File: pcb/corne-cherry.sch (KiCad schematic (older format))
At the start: 144 parts, among them J1 MJ-4PP-9, J2 OLED, J3 MJ-4PP-9, J4 OLED, J5 Conn_01x01_Male, J6 Conn_01x01_Male, P1 Conn_01x03, P3 Conn_01x03, SW1 SW_PUSH, SW10 SW_PUSH, SW11 SW_PUSH, SW12 SW_PUSH, SW13 SW_PUSH, SW14 SW_PUSH, SW15 SW_PUSH, SW16 SW_PUSH, SW17 SW_PUSH, SW18 SW_PUSH, SW19 SW_PUSH, SW2 SW_PUSH, SW20 SW_PUSH, SW21 SW_PUSH, SW22 SW_PUSH, SW23 SW_PUSH, SW24 SW_PUSH, SW25 SW_PUSH, SW26 SW_PUSH, SW27 SW_PUSH, SW28 SW_PUSH, SW29 SW_PUSH, SW3 SW_PUSH, SW30 SW_PUSH, SW31 SW_PUSH, SW32 SW_PUSH, SW33 SW_PUSH, SW34 SW_PUSH, SW35 SW_PUSH, SW36 SW_PUSH, SW37 SW_PUSH, SW38 SW_PUSH, SW39 SW_PUSH, SW4 SW_PUSH, SW40 SW_PUSH, SW41 SW_PUSH, SW42 SW_PUSH, SW5 SW_PUSH, SW6 SW_PUSH, SW7 SW_PUSH, SW8 SW_PUSH, SW9 SW_PUSH, U1 ProMicro, U2 ProMicro

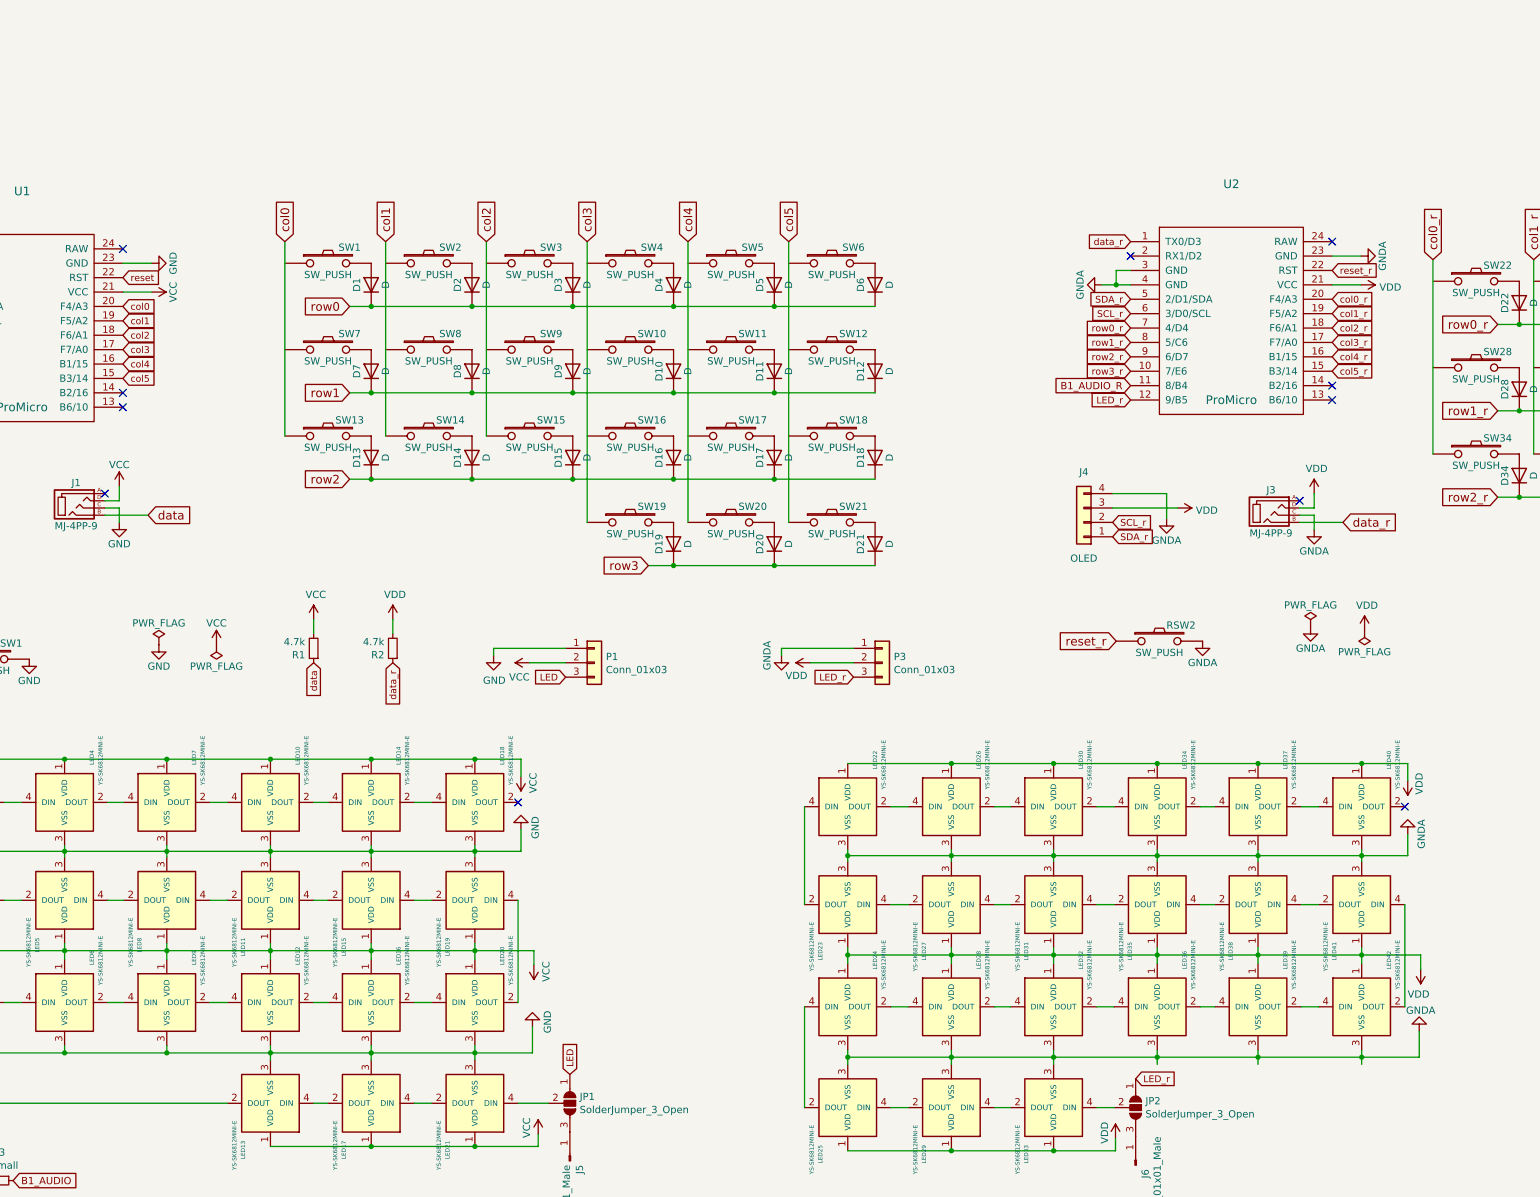
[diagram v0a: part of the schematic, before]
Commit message: Add encoder to left half
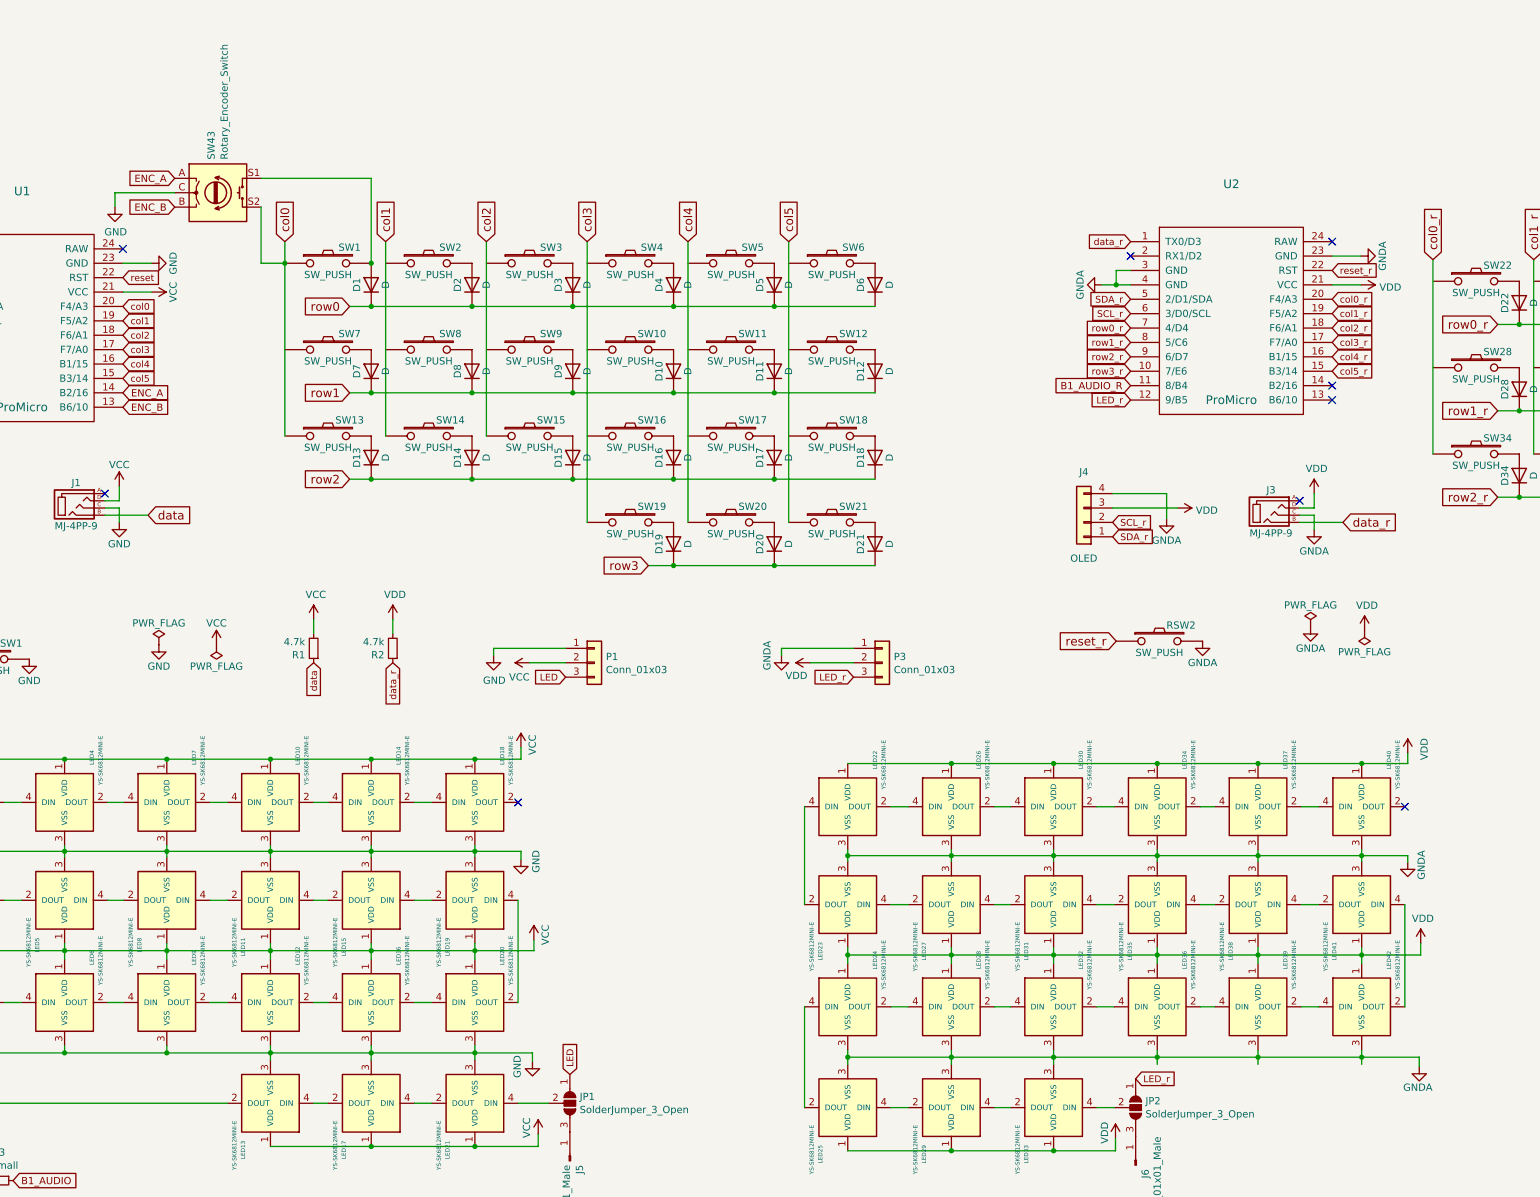
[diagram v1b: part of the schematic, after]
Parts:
- added SW43: Rotary_Encoder_Switch, Keebio-Parts:RotaryEncoder_EC11-no-legs, symbol Device:Rotary_Encoder_Switch
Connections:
- net GND: now also SW43.C
- net col0: now also SW1.1, SW43.S2
- net ENC_B: now reaches U1.13 (B6/10)
- net ENC_B: now also SW43.B
- net ENC_A: now reaches U1.14 (B2/16)
- net ENC_A: now also SW43.A
- net at D1.2 (A), SW1.2: now also SW43.S1
- no-connect marks 15 -> 13
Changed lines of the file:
@@
 Text GLabel 2475 1575 2    47   Input ~ 0
 col0
-NoConn ~ 2475 2175
 Text GLabel 1075 1575 0    47   Input ~ 0
 SDA
@@
 	9725 2875 9725 3050
 Wire Wire Line
-	3600 1125 3600 2475
+	3600 1125 3600 1275
 Wire Wire Line
 	4300 1125 4300 2475
@@
 $EndComp
 $Comp
-L kbd:YS-SK6812MINI-E LED20
-U 1 1 60615E90
-P 4920 6410
-F 0 "LED20" V 5110 6670 29  0000 L CNN
-F 1 "YS-SK6812MINI-E" V 5170 6530 29  0000 L CNN
-F 2 "kbd:YS-SK6812MINI-E" H 5020 6160 50  0001 C CNN
-F 3 "" H 5020 6160 50  0001 C CNN
-	1    4920 6410
-	1    0    0    -1
-$EndComp
-$Comp
 L kbd:YS-SK6812MINI-E LED16
 U 1 1 60615E86
@@
 	1350 5360 2070 5360
 Wire Wire Line
-	5240 5360 5240 5210
-Wire Wire Line
 	4920 5320 4920 5360
 Connection ~ 4920 5360
@@
 Wire Wire Line
 	1350 4720 2070 4720
-Wire Wire Line
-	5240 4720 5240 4840
 Connection ~ 2070 4720
 Wire Wire Line
@@
 L power:VCC #PWR0107
 U 1 1 607BF7C1
-P 5240 4840
-F 0 "#PWR0107" H 5240 4690 50  0001 C CNN
-F 1 "VCC" V 5155 4885 50  0000 C CNN
-F 2 "" H 5240 4840 50  0001 C CNN
-F 3 "" H 5240 4840 50  0001 C CNN
-	1    5240 4840
-	-1   0    0    1
+P 5240 4640
+F 0 "#PWR0107" H 5240 4490 50  0001 C CNN
+F 1 "VCC" V 5320 4660 50  0000 C CNN
+F 2 "" H 5240 4640 50  0001 C CNN
+F 3 "" H 5240 4640 50  0001 C CNN
+	1    5240 4640
+	1    0    0    -1
 $EndComp
 $Comp
 L power:GND #PWR0108
 U 1 1 607C08F0
-P 5240 5210
-F 0 "#PWR0108" H 5240 4960 50  0001 C CNN
-F 1 "GND" V 5140 5195 50  0000 C CNN
-F 2 "" H 5240 5210 50  0001 C CNN
-F 3 "" H 5240 5210 50  0001 C CNN
-	1    5240 5210
-	-1   0    0    1
+P 5240 5415
+F 0 "#PWR0108" H 5240 5165 50  0001 C CNN
+F 1 "GND" V 5345 5400 50  0000 C CNN
+F 2 "" H 5240 5415 50  0001 C CNN
+F 3 "" H 5240 5415 50  0001 C CNN
+	1    5240 5415
+	1    0    0    -1
 $EndComp
 Wire Wire Line
 	1350 6050 2070 6050
-Wire Wire Line
-	5330 6050 5330 6150
 Wire Wire Line
 	1350 6710 1350 6760
@@
 Wire Wire Line
 	4920 6760 5320 6760
-Wire Wire Line
-	5320 6760 5320 6580
 $Comp
 L power:VCC #PWR0109
 U 1 1 60A1725F
-P 5330 6150
-F 0 "#PWR0109" H 5330 6000 50  0001 C CNN
-F 1 "VCC" V 5245 6195 50  0000 C CNN
-F 2 "" H 5330 6150 50  0001 C CNN
-F 3 "" H 5330 6150 50  0001 C CNN
-	1    5330 6150
-	-1   0    0    1
-$EndComp
-$Comp
-L power:GND #PWR0110
-U 1 1 60A183F3
-P 5320 6580
-F 0 "#PWR0110" H 5320 6330 50  0001 C CNN
-F 1 "GND" V 5215 6545 50  0000 C CNN
-F 2 "" H 5320 6580 50  0001 C CNN
-F 3 "" H 5320 6580 50  0001 C CNN
-	1    5320 6580
-	-1   0    0    1
+P 5330 5975
+F 0 "#PWR0109" H 5330 5825 50  0001 C CNN
+F 1 "VCC" V 5410 6010 50  0000 C CNN
+F 2 "" H 5330 5975 50  0001 C CNN
+F 3 "" H 5330 5975 50  0001 C CNN
+	1    5330 5975
+	1    0    0    -1
 $EndComp
 Wire Wire Line
@@
 Wire Wire Line
 	7510 4750 8230 4750
-Wire Wire Line
-	11400 4750 11400 4870
 Connection ~ 8230 4750
 Wire Wire Line
@@
 	7510 6080 8230 6080
 Wire Wire Line
-	11490 6080 11490 6180
-Wire Wire Line
 	7510 6740 7510 6790
 Wire Wire Line
@@
 Wire Wire Line
 	11080 6790 11480 6790
-Wire Wire Line
-	11480 6790 11480 6610
 Wire Wire Line
 	10780 6440 10660 6440
@@
 L power:VDD #PWR0112
 U 1 1 60837821
-P 11490 6180
-F 0 "#PWR0112" H 11490 6030 50  0001 C CNN
-F 1 "VDD" H 11505 6353 50  0000 C CNN
-F 2 "" H 11490 6180 50  0001 C CNN
-F 3 "" H 11490 6180 50  0001 C CNN
-	1    11490 6180
-	-1   0    0    1
+P 11490 6000
+F 0 "#PWR0112" H 11490 5850 50  0001 C CNN
+F 1 "VDD" H 11505 6173 50  0000 C CNN
+F 2 "" H 11490 6000 50  0001 C CNN
+F 3 "" H 11490 6000 50  0001 C CNN
+	1    11490 6000
+	1    0    0    -1
 $EndComp
 $Comp
 L power:GNDA #PWR0115
 U 1 1 60878D51
-P 11480 6610
-F 0 "#PWR0115" H 11480 6360 50  0001 C CNN
-F 1 "GNDA" H 11470 6465 50  0000 C CNN
-F 2 "" H 11480 6610 50  0001 C CNN
-F 3 "" H 11480 6610 50  0001 C CNN
-	1    11480 6610
-	-1   0    0    1
-$EndComp
-$Comp
-L power:GNDA #PWR0116
-U 1 1 6087A621
-P 11400 5240
-F 0 "#PWR0116" H 11400 4990 50  0001 C CNN
-F 1 "GNDA" V 11305 5240 50  0000 C CNN
-F 2 "" H 11400 5240 50  0001 C CNN
-F 3 "" H 11400 5240 50  0001 C CNN
-	1    11400 5240
-	-1   0    0    1
+P 11480 6855
+F 0 "#PWR0115" H 11480 6605 50  0001 C CNN
+F 1 "GNDA" H 11470 6710 50  0000 C CNN
+F 2 "" H 11480 6855 50  0001 C CNN
+F 3 "" H 11480 6855 50  0001 C CNN
+	1    11480 6855
+	1    0    0    -1
 $EndComp
 $Comp
@@
 	1    0    0    -1
 $EndComp
-NoConn ~ 2475 2275
 $Comp
 L kbd:ProMicro U2
@@
 	9370 7440 9370 7355
 $Comp
-L power:VDD #PWR?
+L power:VDD #PWR0111
 U 1 1 6082E68A
 P 9370 7355
-F 0 "#PWR?" H 9370 7205 50  0001 C CNN
+F 0 "#PWR0111" H 9370 7205 50  0001 C CNN
 F 1 "VDD" V 9295 7395 50  0000 C CNN
 F 2 "" H 9370 7355 50  0001 C CNN
@@
 	0    1    1    0
 $EndComp
-Wire Wire Line
-	11400 5390 11400 5240
-Wire Wire Line
-	10360 4750 11080 4750
-Wire Wire Line
-	11080 4750 11400 4750
-Connection ~ 11080 4750
 $Comp
 L power:VDD #PWR0114
 U 1 1 60838250
-P 11400 4870
-F 0 "#PWR0114" H 11400 4720 50  0001 C CNN
-F 1 "VDD" V 11320 4890 50  0000 C CNN
-F 2 "" H 11400 4870 50  0001 C CNN
-F 3 "" H 11400 4870 50  0001 C CNN
-	1    11400 4870
-	-1   0    0    1
-$EndComp
+P 11400 4680
+F 0 "#PWR0114" H 11400 4530 50  0001 C CNN
+F 1 "VDD" V 11515 4710 50  0000 C CNN
+F 2 "" H 11400 4680 50  0001 C CNN
+F 3 "" H 11400 4680 50  0001 C CNN
+	1    11400 4680
+	1    0    0    -1
+$EndComp
+Wire Wire Line
+	5360 7410 5360 7325
+$Comp
+L power:VCC #PWR0113
+U 1 1 6098BE6F
+P 5360 7325
+F 0 "#PWR0113" H 5360 7175 50  0001 C CNN
+F 1 "VCC" V 5280 7370 50  0000 C CNN
+F 2 "" H 5360 7325 50  0001 C CNN
+F 3 "" H 5360 7325 50  0001 C CNN
+	1    5360 7325
+	1    0    0    -1
+$EndComp
+$Comp
+L power:GND #PWR0110
+U 1 1 60A183F3
+P 5320 6820
+F 0 "#PWR0110" H 5320 6570 50  0001 C CNN
+F 1 "GND" V 5215 6785 50  0000 C CNN
+F 2 "" H 5320 6820 50  0001 C CNN
+F 3 "" H 5320 6820 50  0001 C CNN
+	1    5320 6820
+	1    0    0    -1
+$EndComp
+$Comp
+L kbd:YS-SK6812MINI-E LED20
+U 1 1 60615E90
+P 4920 6410
+F 0 "LED20" V 5110 6670 29  0000 L CNN
+F 1 "YS-SK6812MINI-E" V 5170 6530 29  0000 L CNN
+F 2 "kbd:YS-SK6812MINI-E" H 5020 6160 50  0001 C CNN
+F 3 "" H 5020 6160 50  0001 C CNN
+	1    4920 6410
+	1    0    0    -1
+$EndComp
+Wire Wire Line
+	5320 6760 5320 6820
+Wire Wire Line
+	5330 6050 5330 5975
+Wire Wire Line
+	5240 5360 5240 5415
+Wire Wire Line
+	5240 4720 5240 4640
+Wire Wire Line
+	11480 6855 11480 6790
+Wire Wire Line
+	11490 6080 11490 6000
+Connection ~ 11080 4750
+Wire Wire Line
+	11080 4750 11400 4750
+Wire Wire Line
+	10360 4750 11080 4750
 $Comp
 L kbd:YS-SK6812MINI-E LED40
@@
 	1    0    0    -1
 $EndComp
-Wire Wire Line
-	5360 7410 5360 7325
-$Comp
-L power:VCC #PWR?
-U 1 1 6098BE6F
-P 5360 7325
-F 0 "#PWR?" H 5360 7175 50  0001 C CNN
-F 1 "VCC" V 5280 7370 50  0000 C CNN
-F 2 "" H 5360 7325 50  0001 C CNN
-F 3 "" H 5360 7325 50  0001 C CNN
-	1    5360 7325
-	1    0    0    -1
-$EndComp
+$Comp
+L power:GNDA #PWR0116
+U 1 1 6087A621
+P 11400 5435
+F 0 "#PWR0116" H 11400 5185 50  0001 C CNN
+F 1 "GNDA" V 11495 5415 50  0000 C CNN
+F 2 "" H 11400 5435 50  0001 C CNN
+F 3 "" H 11400 5435 50  0001 C CNN
+	1    11400 5435
+	1    0    0    -1
+$EndComp
+Wire Wire Line
+	11400 5390 11400 5435
+Wire Wire Line
+	11400 4750 11400 4680
+$Comp
+L Device:Rotary_Encoder_Switch SW43
+U 1 1 6078866B
+P 3135 785
+F 0 "SW43" V 3089 1015 50  0000 L CNN
+F 1 "Rotary_Encoder_Switch" V 3180 1015 50  0000 L CNN
+F 2 "Keebio-Parts:RotaryEncoder_EC11-no-legs" H 2985 945 50  0001 C CNN
+F 3 "~" H 3135 1045 50  0001 C CNN
+	1    3135 785
+	1    0    0    -1
+$EndComp
+Wire Wire Line
+	2835 785  2420 785
+Wire Wire Line
+	2420 785  2420 885
+$Comp
+L power:GND #PWR?
+U 1 1 60823858
+P 2420 885
+F 0 "#PWR?" H 2420 635 50  0001 C CNN
+F 1 "GND" H 2425 712 50  0000 C CNN
+F 2 "" H 2420 885 50  0001 C CNN
+F 3 "" H 2420 885 50  0001 C CNN
+	1    2420 885
+	1    0    0    -1
+$EndComp
+Text GLabel 2835 685  0    50   Input ~ 0
+ENC_A
+Text GLabel 2835 885  0    50   Input ~ 0
+ENC_B
+Text GLabel 2475 2275 2    50   Input ~ 0
+ENC_B
+Text GLabel 2475 2175 2    50   Input ~ 0
+ENC_A
+Wire Wire Line
+	3435 885  3435 1275
+Wire Wire Line
+	3435 1275 3600 1275
+Connection ~ 3600 1275
+Wire Wire Line
+	3600 1275 3600 2475
+Wire Wire Line
+	3435 685  4200 685
+Wire Wire Line
+	4200 685  4200 1275
+Connection ~ 4200 1275
 $EndSCHEMATC

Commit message: Finish PCB
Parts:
- added SW44: Rotary_Encoder_Switch, Keebio-Parts:RotaryEncoder_EC11-no-legs, symbol Device:Rotary_Encoder_Switch
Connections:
- net GNDA: now also SW44.C
- net col0_r: now also SW22.1, SW44.S2
- net ENC_B_R: now reaches U2.13 (B6/10)
- net ENC_B_R: now also SW44.B
- net ENC_A_R: now reaches U2.14 (B2/16)
- net ENC_A_R: now also SW44.A
- net at D22.2 (A), SW22.2: now also SW44.S1
- no-connect marks 13 -> 11
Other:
- moved on the sheet: U2
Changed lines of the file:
@@
 L power:GNDA #PWR017
 U 1 1 5C25F963
-P 11075 1225
-F 0 "#PWR017" H 11075 975 50  0001 C CNN
-F 1 "GNDA" H 11075 1075 50  0000 C CNN
-F 2 "" H 11075 1225 50  0001 C CNN
-F 3 "" H 11075 1225 50  0001 C CNN
-	1    11075 1225
+P 10105 1250
+F 0 "#PWR017" H 10105 1000 50  0001 C CNN
+F 1 "GNDA" H 10105 1100 50  0000 C CNN
+F 2 "" H 10105 1250 50  0001 C CNN
+F 3 "" H 10105 1250 50  0001 C CNN
+	1    10105 1250
 	0    -1   -1   0
 $EndComp
@@
 L power:GNDA #PWR018
 U 1 1 5C25F969
-P 9275 1425
-F 0 "#PWR018" H 9275 1175 50  0001 C CNN
-F 1 "GNDA" H 9275 1275 50  0000 C CNN
-F 2 "" H 9275 1425 50  0001 C CNN
-F 3 "" H 9275 1425 50  0001 C CNN
-	1    9275 1425
+P 8305 1450
+F 0 "#PWR018" H 8305 1200 50  0001 C CNN
+F 1 "GNDA" H 8305 1300 50  0000 C CNN
+F 2 "" H 8305 1450 50  0001 C CNN
+F 3 "" H 8305 1450 50  0001 C CNN
+	1    8305 1450
 	0    1    1    0
 $EndComp
-Text GLabel 10875 1625 2    47   Input ~ 0
+Text GLabel 9905 1650 2    47   Input ~ 0
 col1_r
-Text GLabel 10875 1725 2    47   Input ~ 0
+Text GLabel 9905 1750 2    47   Input ~ 0
 col2_r
-Text GLabel 10875 1825 2    47   Input ~ 0
+Text GLabel 9905 1850 2    47   Input ~ 0
 col3_r
-Text GLabel 10875 1925 2    47   Input ~ 0
+Text GLabel 9905 1950 2    47   Input ~ 0
 col4_r
-Text GLabel 10875 2025 2    47   Input ~ 0
+Text GLabel 9905 2050 2    47   Input ~ 0
 col5_r
-Text GLabel 9475 2025 0    47   Input ~ 0
+Text GLabel 8505 2050 0    47   Input ~ 0
 row3_r
-Text GLabel 9475 1925 0    47   Input ~ 0
+Text GLabel 8505 1950 0    47   Input ~ 0
 row2_r
-Text GLabel 9475 1825 0    47   Input ~ 0
+Text GLabel 8505 1850 0    47   Input ~ 0
 row1_r
-Text GLabel 9475 1725 0    47   Input ~ 0
+Text GLabel 8505 1750 0    47   Input ~ 0
 row0_r
 $Comp
@@
 	1    0    0    -1
 $EndComp
-Text GLabel 9475 2225 0    47   Input ~ 0
+Text GLabel 8505 2250 0    47   Input ~ 0
 LED_r
-Text GLabel 9475 1125 0    47   Input ~ 0
+Text GLabel 8505 1150 0    47   Input ~ 0
 data_r
 $Comp
@@
 Text GLabel 10950 3075 2    60   Input ~ 0
 data_r
-Text GLabel 10875 1325 2    47   Input ~ 0
+Text GLabel 9905 1350 2    47   Input ~ 0
 reset_r
 Text GLabel 9375 3900 0    60   Input ~ 0
 reset_r
-NoConn ~ 9475 1225
-Text GLabel 10875 1525 2    47   Input ~ 0
+NoConn ~ 8505 1250
+Text GLabel 9905 1550 2    47   Input ~ 0
 col0_r
-NoConn ~ 10875 2125
-Text GLabel 9475 1525 0    47   Input ~ 0
+Text GLabel 8505 1550 0    47   Input ~ 0
 SDA_r
-Text GLabel 9475 1625 0    47   Input ~ 0
+Text GLabel 8505 1650 0    47   Input ~ 0
 SCL_r
 $Comp
@@
 Text GLabel 9350 3175 2    47   Input ~ 0
 SDA_r
-NoConn ~ 10875 1125
+NoConn ~ 9905 1150
 $Comp
 L kbd:MJ-4PP-9 J3
@@
 	12025 1700 12175 1700
 Wire Wire Line
-	9375 1325 9375 1425
-Connection ~ 9375 1425
-Wire Wire Line
-	9475 1325 9375 1325
-Wire Wire Line
-	9275 1425 9375 1425
+	8405 1350 8405 1450
+Connection ~ 8405 1450
+Wire Wire Line
+	8505 1350 8405 1350
+Wire Wire Line
+	8305 1450 8405 1450
 Connection ~ 12175 2900
 Connection ~ 12875 2900
@@
 Connection ~ 14975 1700
 Wire Wire Line
-	10875 1225 11075 1225
-Wire Wire Line
-	10875 1425 11075 1425
+	9905 1250 10105 1250
+Wire Wire Line
+	9905 1450 10105 1450
 Wire Wire Line
 	10650 3075 10950 3075
@@
 	14975 3500 15675 3500
 Wire Wire Line
-	9375 1425 9475 1425
+	8405 1450 8505 1450
 Wire Wire Line
 	12175 2900 12875 2900
@@
 L power:VDD #PWR019
 U 1 1 5C714C7F
-P 11075 1425
-F 0 "#PWR019" H 11075 1275 50  0001 C CNN
-F 1 "VDD" V 11092 1553 50  0000 L CNN
-F 2 "" H 11075 1425 50  0001 C CNN
-F 3 "" H 11075 1425 50  0001 C CNN
-	1    11075 1425
+P 10105 1450
+F 0 "#PWR019" H 10105 1300 50  0001 C CNN
+F 1 "VDD" V 10122 1578 50  0000 L CNN
+F 2 "" H 10105 1450 50  0001 C CNN
+F 3 "" H 10105 1450 50  0001 C CNN
+	1    10105 1450
 	0    1    1    0
 $EndComp
@@
 	5000 1125 5000 2475
 Wire Wire Line
-	11575 1250 11575 2600
+	11575 1250 11575 1400
 Wire Wire Line
 	12275 1250 12275 2600
@@
 L kbd:ProMicro U2
 U 1 1 5C25F857
-P 10175 1675
-F 0 "U2" H 10175 2625 60  0000 C CNN
-F 1 "ProMicro" H 10175 1125 60  0000 C CNN
-F 2 "kbd:ProMicro_v3" H 10275 625 60  0001 C CNN
-F 3 "" H 10275 625 60  0000 C CNN
-	1    10175 1675
-	1    0    0    -1
-$EndComp
-NoConn ~ 10875 2225
+P 9205 1700
+F 0 "U2" H 9205 2650 60  0000 C CNN
+F 1 "ProMicro" H 9205 1150 60  0000 C CNN
+F 2 "kbd:ProMicro_v3" H 9305 650 60  0001 C CNN
+F 3 "" H 9305 650 60  0000 C CNN
+	1    9205 1700
+	1    0    0    -1
+$EndComp
 NoConn ~ 5718 9687
 NoConn ~ 5470 8376
@@
 Wire Wire Line
 	7467 8158 7467 8302
-Text GLabel 9475 2125 0    50   Input ~ 0
+Text GLabel 8505 2150 0    50   Input ~ 0
 B1_AUDIO_R
 Text GLabel 1712 7647 2    50   Input ~ 0
@@
 	2420 785  2420 885
 $Comp
-L power:GND #PWR?
+L power:GND #PWR0119
 U 1 1 60823858
 P 2420 885
-F 0 "#PWR?" H 2420 635 50  0001 C CNN
+F 0 "#PWR0119" H 2420 635 50  0001 C CNN
 F 1 "GND" H 2425 712 50  0000 C CNN
 F 2 "" H 2420 885 50  0001 C CNN
@@
 	4200 685  4200 1275
 Connection ~ 4200 1275
+Text GLabel 9905 2150 2    50   Input ~ 0
+ENC_A_R
+Text GLabel 9905 2250 2    50   Input ~ 0
+ENC_B_R
+$Comp
+L Device:Rotary_Encoder_Switch SW44
+U 1 1 60786552
+P 11045 930
+F 0 "SW44" H 11045 1297 50  0000 C CNN
+F 1 "Rotary_Encoder_Switch" H 11045 1206 50  0000 C CNN
+F 2 "Keebio-Parts:RotaryEncoder_EC11-no-legs" H 10895 1090 50  0001 C CNN
+F 3 "~" H 11045 1190 50  0001 C CNN
+	1    11045 930
+	1    0    0    -1
+$EndComp
+Text GLabel 10745 1030 0    50   Input ~ 0
+ENC_B_R
+Text GLabel 10745 830  0    50   Input ~ 0
+ENC_A_R
+Wire Wire Line
+	10745 930  10150 930
+Wire Wire Line
+	10150 930  10150 1030
+$Comp
+L power:GNDA #PWR0120
+U 1 1 607DCD43
+P 10150 1030
+F 0 "#PWR0120" H 10150 780 50  0001 C CNN
+F 1 "GNDA" V 10060 1020 50  0000 C CNN
+F 2 "" H 10150 1030 50  0001 C CNN
+F 3 "" H 10150 1030 50  0001 C CNN
+	1    10150 1030
+	1    0    0    -1
+$EndComp
+Wire Wire Line
+	11345 830  12175 830
+Wire Wire Line
+	12175 830  12175 1400
+Connection ~ 12175 1400
+Wire Wire Line
+	11345 1030 11345 1400
+Wire Wire Line
+	11345 1400 11575 1400
+Connection ~ 11575 1400
+Wire Wire Line
+	11575 1400 11575 2600
 $EndSCHEMATC
